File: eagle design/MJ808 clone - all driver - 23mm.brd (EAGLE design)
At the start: 23 x 23 mm, 32 parts, among them IC1 ATTINY4313-MMH, IC2 PRQV8.00CR1510Y00L, IC3 MCP2515, IC5 MCP2561-2, IC6 MAX16820, IC7 LDK320ADU50R, Q2 SiA456DJ, SW1 TL3305-844809

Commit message: - further work on mj808 23mm pcb
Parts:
- removed R14: 741X083103JP 10k, 74x-1133528 Resistor Array:0402
- moved R11 2.90 mm to (-2.90, -8.00)
- moved C2 1.25 mm to (-6.95, 0.20), turned to 180 degrees
- moved C1 0.76 mm to (-0.85, 4.00)
- moved C5 0.75 mm to (-6.95, 1.30), turned to 180 degrees
- moved C6 0.54 mm to (1.20, 8.50)
- moved D1 0.50 mm to (-4.30, -4.65)
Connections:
- net 5V0: no longer R14.1, R14.3, R14.7
- net DIM_FRONT: no longer R14.6
- net GND: no longer R14.5
- net RESET: no longer R14.4
- net SPI_SS: no longer R14.8
- net STBY: no longer R14.2
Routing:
- net GND: track 2.43 -> 10.2 mm, vias 1 -> 8
- net CANL: track 10.0 -> 6.83 mm
- net CANH: track 9.91 -> 7.01 mm
- net 5V0: track 37.5 -> 34.7 mm
- net GREEN_LED: track 9.88 -> 8.18 mm
- net RED_LED: track 8.82 -> 7.50 mm
- net LED_AN: track 11.2 -> 10.2 mm
- net RXCAN: track 4.31 -> 5.35 mm
- net SPI_SS: track 17.3 -> 18.2 mm
- net SPI_MISO: track 9.21 -> 10.0 mm
- added copper zone on layer 1, net GND
- added copper zone on layer 15, net GND
- added copper zone on layer 16, net GND
- added copper zone on layer 2, net GND

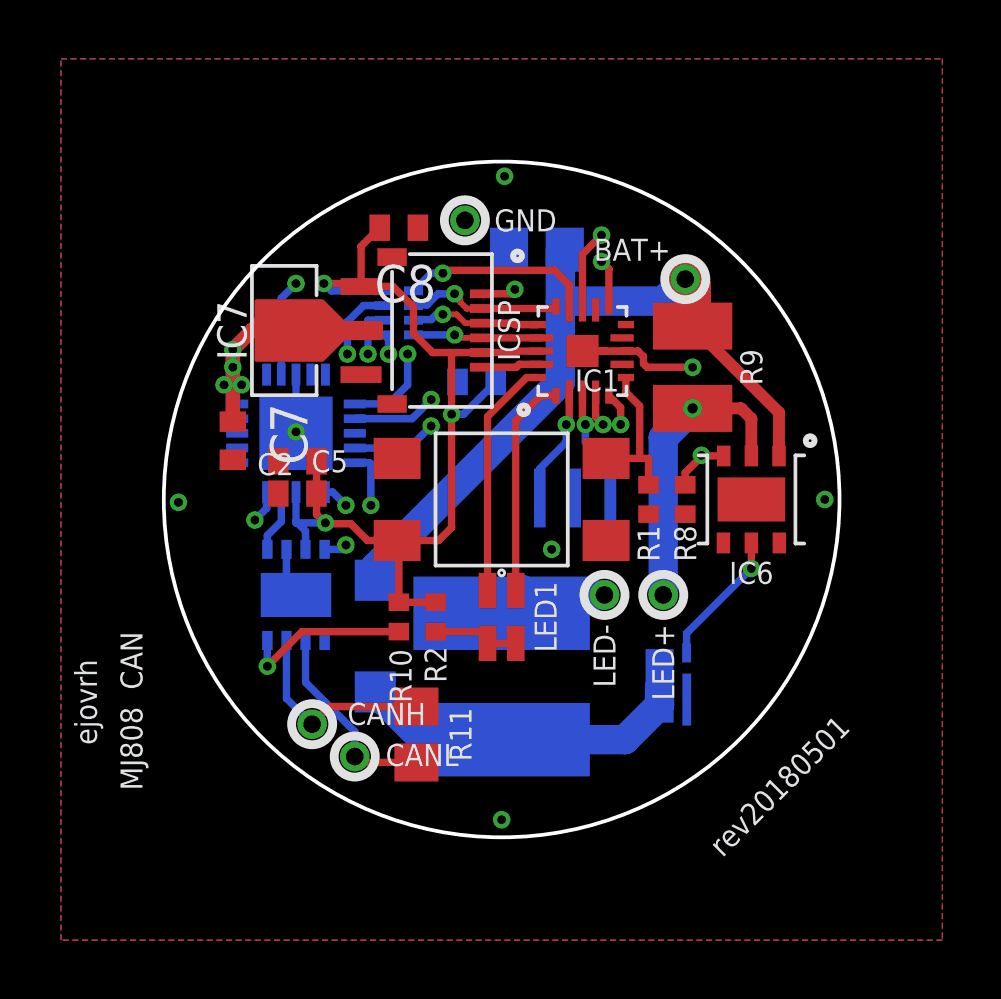
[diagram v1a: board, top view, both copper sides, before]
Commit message: - synced POC board with production board - corrected name and value placements on both boards - work on production board still continues
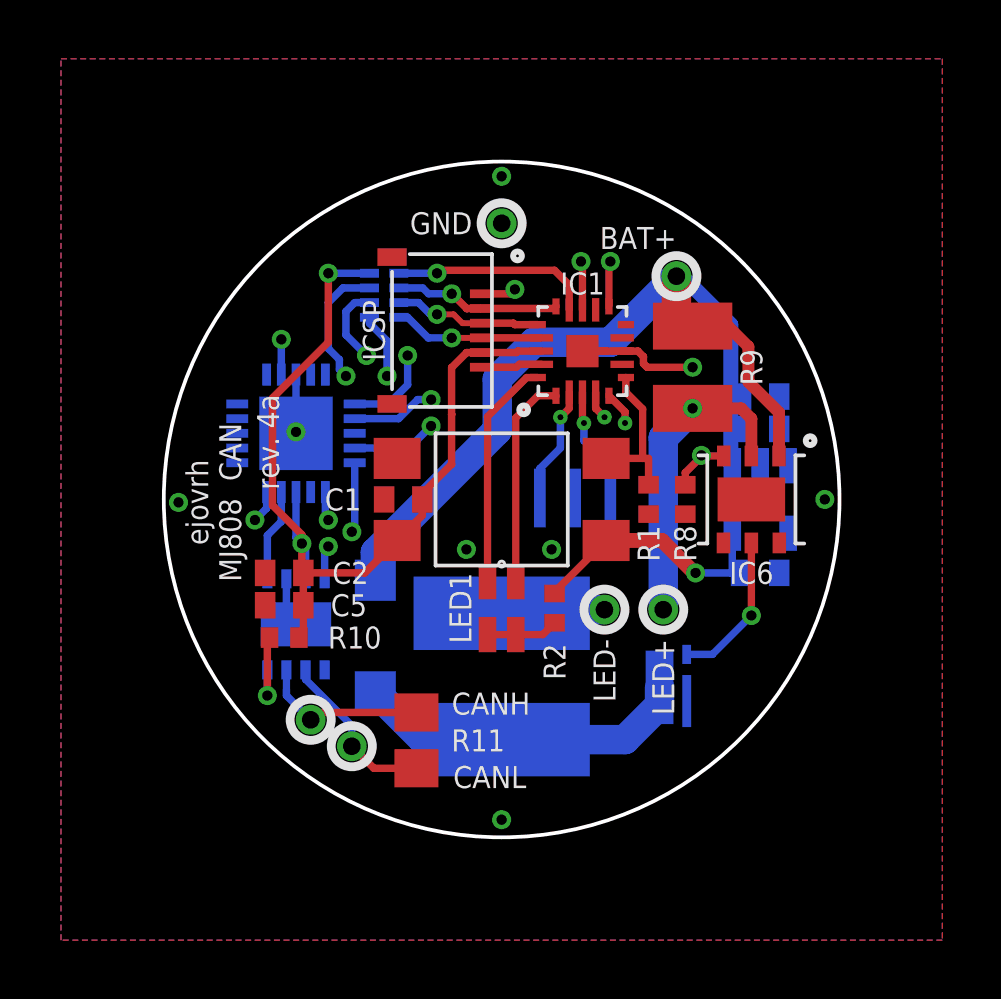
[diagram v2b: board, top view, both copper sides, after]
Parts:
- C6: device rcl:C0805 -> rcl:C0402
- C7: value 1μF -> 1μF / 10V
- IC7: device LDO SOT-89:SOT-89 -> LDK320 5V LDO:SOT-23-5L
- moved C7 18.0 mm to (8.80, 2.40), flipped to the bottom, turned to 180 degrees
- moved C8 17.0 mm to (8.80, -2.50), flipped to the bottom, turned to 0 degrees
- moved IC7 14.1 mm to (8.80, 0.00), flipped to the bottom, turned to 0 degrees
- moved C6 9.10 mm to (8.80, 3.50), turned to 180 degrees
- moved C5 4.92 mm to (-7.40, -3.60)
- moved C1 4.72 mm to (-3.35, 0.00), flipped to the top, turned to 180 degrees
- moved R2 4.06 mm to (1.80, -3.70)
- moved R10 3.96 mm to (-7.40, -4.70), turned to 180 degrees
- moved C2 2.74 mm to (-7.40, -2.50)
- moved GND 1.25 mm to (0.00, 9.40)
- moved IC5 1.00 mm to (-7.00, -4.25)
- moved R13 0.78 mm to (-4.00, 6.95)
- moved LED+ 0.50 mm to (5.50, -3.75)
- moved LED- 0.50 mm to (3.50, -3.75)
- moved CANL 0.36 mm to (-5.10, -8.40)
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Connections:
- net 5V0: now also IC7.OUT; no longer IC7.VOUT
- net BAT+: now also IC7.IN; no longer IC7.VIN
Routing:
- net BAT+: track 58.1 -> 32.4 mm, vias 4 -> 0
- net 5V0: track 34.7 -> 41.1 mm
- net CLOCKOUT: track 17.4 -> 14.7 mm
- net SPI_MISO: track 10.0 -> 12.1 mm
- net DIM_FRONT: track 14.0 -> 12.0 mm
- net STBY: track 26.0 -> 24.0 mm
- net SPI_MOSI: track 7.95 -> 9.41 mm
- net CANH: track 7.01 -> 5.75 mm
- net SPI_SCK: track 5.73 -> 6.95 mm
- net CANL: track 6.83 -> 5.76 mm
- net TXCAN: track 2.15 -> 3.15 mm
- net ICSP_DI/MISO: track 5.31 -> 6.13 mm
- net RXCAN: track 5.35 -> 6.17 mm
- net ICSP_SCK: track 4.39 -> 5.14 mm
- net LED: track 3.13 -> 2.55 mm
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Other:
- board text added: "ejovrh MJ808 CAN"
- board text added: "rev. 4a"
- board text removed: "MJ808 CAN"
- board text removed: "ejovrh"
- board text removed: "rev20180501"

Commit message: - further work on PCB layout
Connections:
- net BAT+: now also IC7.EN
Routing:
- net BAT+: track 32.4 -> 36.6 mm
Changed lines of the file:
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@@
 <wire x1="6.5" y1="5.9" x2="5.95" y2="6.45" width="1" layer="1"/>
 <wire x1="5.95" y1="6.45" x2="5.95" y2="7.6" width="1" layer="1"/>
+<contactref element="IC7" pad="EN"/>
+<wire x1="7.85" y1="1.15" x2="7.85" y2="0" width="0.254" layer="16"/>
+<wire x1="7.85" y1="0" x2="9.75" y2="0" width="0.254" layer="16"/>
+<wire x1="9.75" y1="0" x2="9.75" y2="1.15" width="0.254" layer="16"/>
 </signal>
 <signal name="LED_AN">

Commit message: - added mj808 prod board gerber files
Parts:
- moved C2 0.27 mm to (-7.50, -2.75)
- moved C5 0.18 mm to (-7.50, -3.75)
- moved C7 0.11 mm to (8.75, 2.50)
- moved R11 0.11 mm to (-3.00, -8.25)
- moved Q2 0.11 mm to (5.75, -6.50)
- moved R10 0.11 mm to (-7.50, -4.75)
- moved R2 0.07 mm to (1.75, -3.75)
- moved C6 0.05 mm to (8.75, 3.50)
- moved C8 0.05 mm to (8.75, -2.50)
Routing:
- net SPI_SCK: track 6.95 -> 5.26 mm, vias 2 -> 0
- net GND: track 10.2 -> 11.0 mm, vias 9 -> 10
- net RXCAN: track 6.17 -> 5.59 mm

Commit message: - finished mj808 23mm PCB - 4 layer
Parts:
- added R3: 10k, rcl:R0402
- turned Q2 to 270 degrees
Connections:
- net 5V0: now also IC1.18, R3.1; no longer IC1.VCC
- net CLOCKOUT: now also IC1.4; no longer IC1.PD2
- net DEBUGWIRE/RESET: now also IC1.19; no longer IC1.PA2
- net DIM_FRONT: now also IC1.13; no longer IC1.PB3
- net DIM_FRONT_DRAIN: now also Q2.1D, Q2.2D, Q2.5D, Q2.6D
- net DIM_FRONT_GATE: now also Q2.3G; no longer Q2.G
- net GND: now also IC1.8, Q2.4S; no longer IC1.GND1
- net GREEN_LED: now also IC1.20; no longer IC1.PD0
- net ICSP_DI/MISO: now also IC1.15; no longer IC1.PB5
- net ICSP_DO/MOSI: now also IC1.16; no longer IC1.PB6
- net ICSP_SCK: now also IC1.17; no longer IC1.PB7
- net INT: now also IC1.5; no longer IC1.PD3
- net N$1: now also IC1.9; no longer IC1.PD6
- net N$2: now also IC1.7; no longer IC1.PD5
- net N$3: now also IC1.12; no longer IC1.PB2
- net N$4: now also IC1.10; no longer IC1.PB0
- net RED_LED: now also IC1.1; no longer IC1.PD1
- net RESET: now also R3.2
- net SPI_SS: now also IC1.14; no longer IC1.PB4
- net STBY: now also IC1.11; no longer IC1.PB1
- net SWITCH: now also IC1.6; no longer IC1.PD4
- net XTAL1: now also IC1.3; no longer IC1.PA0
- net XTAL2: now also IC1.2; no longer IC1.PA1
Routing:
- net SPI_MISO: track 12.1 -> 8.93 mm
- net RESET: track 0.00 -> 2.21 mm, vias 0 -> 1
- net RXCAN: track 5.59 -> 6.21 mm
- net SPI_SS: track 18.6 -> 19.2 mm
